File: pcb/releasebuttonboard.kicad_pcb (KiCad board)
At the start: 2 copper layers, 65 x 56 mm, 30 parts, among them SW1 ROTENC, U1 24C16, U2 RASPIPLUSHEADER, U3 OLEDHeader, U4 REncHeader, U5 BtnHeader, U6 PAM8407, U7 REncHeader

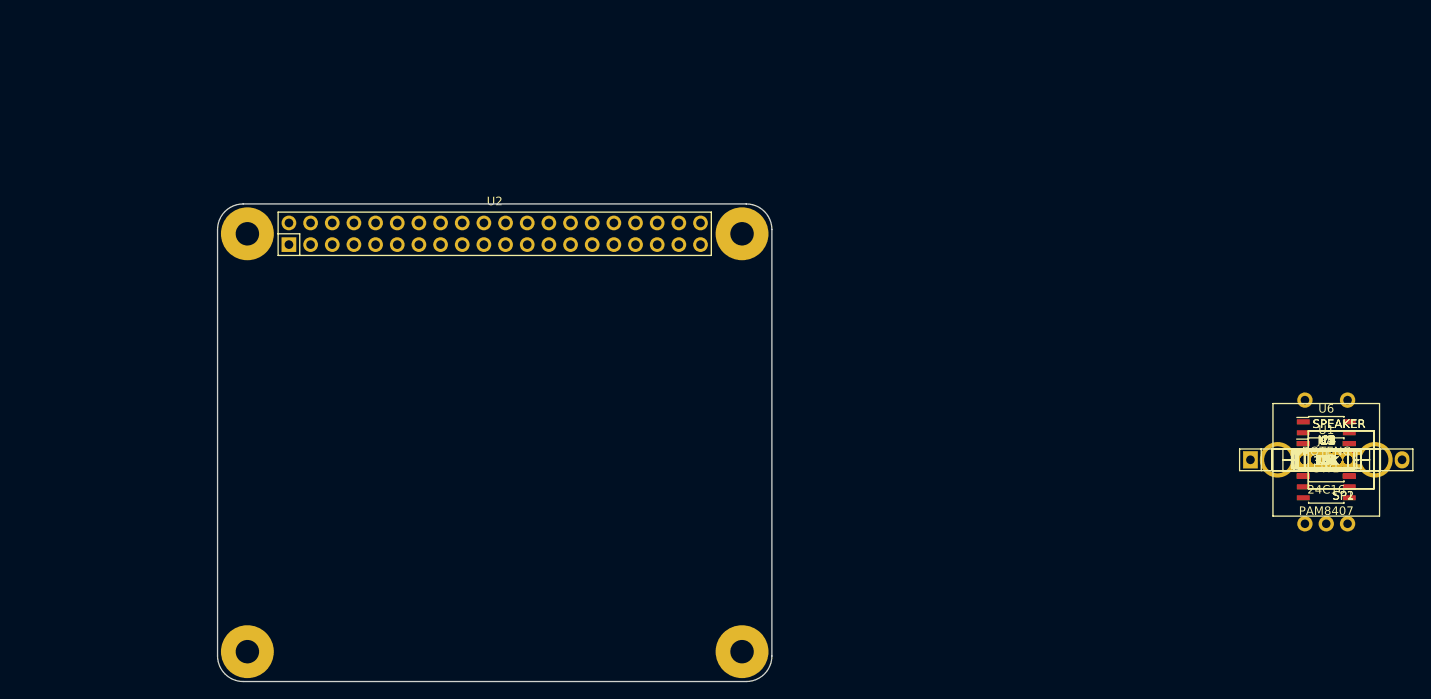
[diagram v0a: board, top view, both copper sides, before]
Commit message: Initial component layout for the audio part of the PCB.
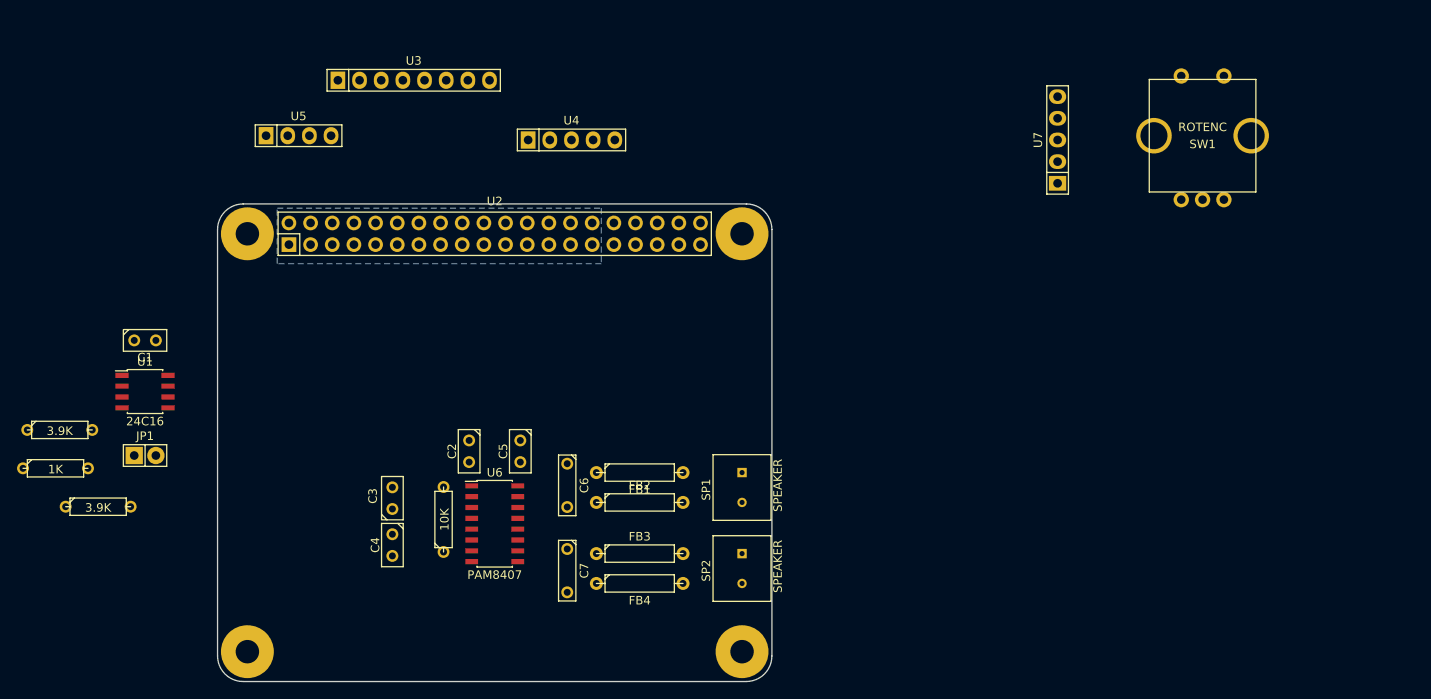
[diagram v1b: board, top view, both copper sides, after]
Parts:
- moved R1 149.0 mm to (76.5, 99.0)
- moved R2 148.5 mm to (77.0, 94.5)
- moved R3 144.1 mm to (81.5, 103.5)
- moved C1 139.2 mm to (87.0, 84.0)
- moved U1 138.7 mm to (87.0, 90.0)
- moved JP1 138.5 mm to (87.0, 97.5)
- moved U5 126.4 mm to (105.0, 60.0)
- moved U3 115.9 mm to (118.5, 53.5)
- moved C4 110.0 mm to (116.0, 108.0), turned to 270 degrees
- moved C3 109.6 mm to (116.0, 102.5), turned to 90 degrees
- moved R4 103.7 mm to (122.0, 105.0), turned to 90 degrees
- moved C2 100.5 mm to (125.0, 97.0), turned to 270 degrees
- moved U6 97.8 mm to (128.0, 105.5)
- moved U4 96.1 mm to (137.0, 60.5)
- moved C5 94.5 mm to (131.0, 97.0), turned to 270 degrees
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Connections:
- SP1 pad 2: Net-(SP1-Pad2) -> Net-(FB2-Pad2)
- SP2 pad 2: Net-(SP2-Pad2) -> Net-(FB4-Pad2)
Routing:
- added copper zone on B.Cu, net GND

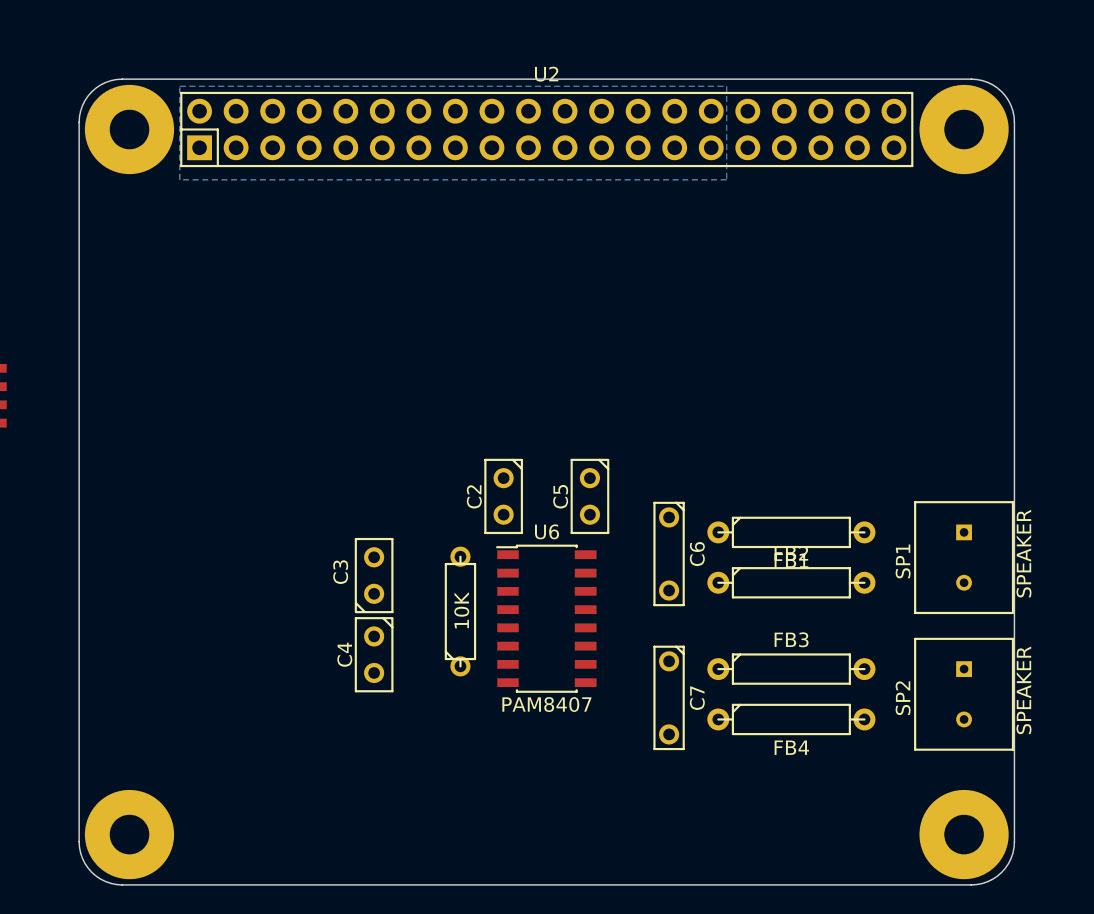
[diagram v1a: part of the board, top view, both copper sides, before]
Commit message: Add separate ground pours for analog and digital.
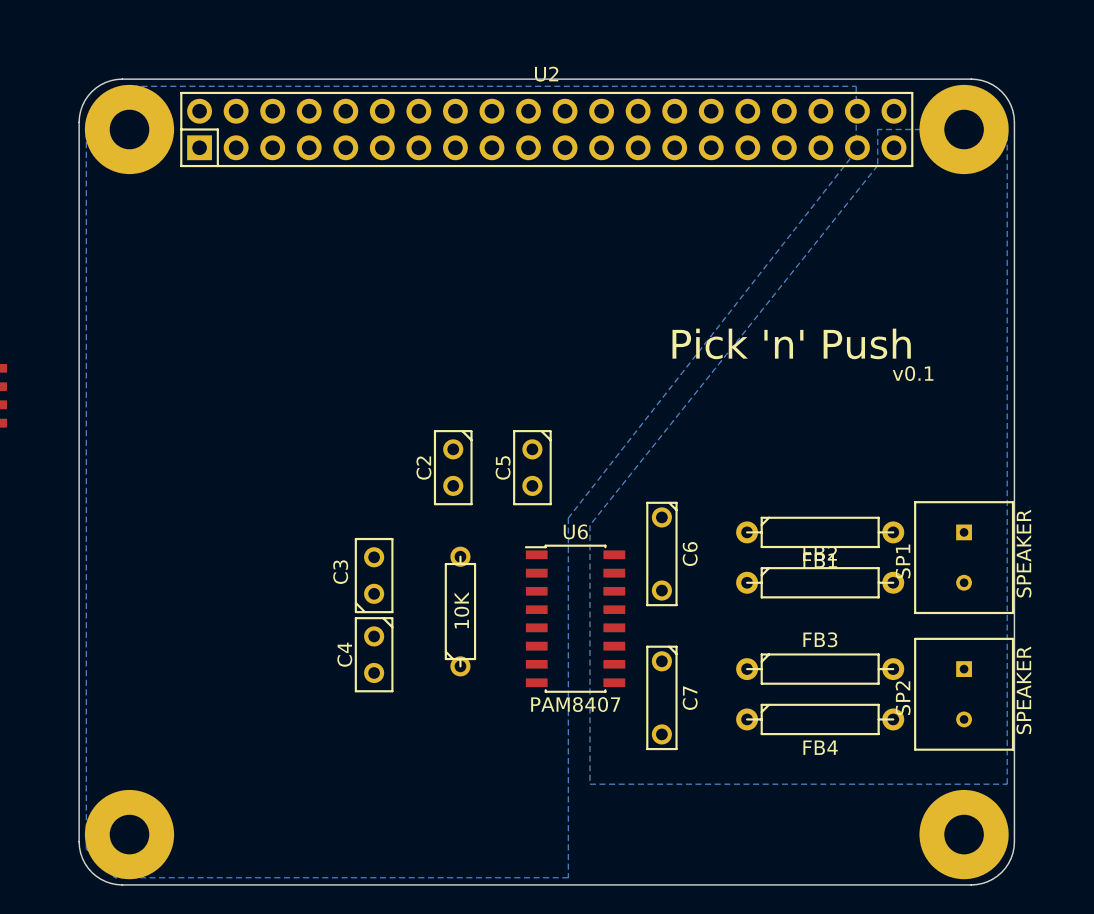
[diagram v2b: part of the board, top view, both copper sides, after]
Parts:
- moved C5 4.47 mm to (127.0, 95.0)
- moved C2 4.03 mm to (121.5, 95.0)
- moved FB1 2.00 mm to (147.0, 99.5)
- moved FB2 2.00 mm to (147.0, 103.0)
- moved FB3 2.00 mm to (147.0, 109.0)
- moved FB4 2.00 mm to (147.0, 112.5)
- moved U6 2.00 mm to (130.0, 105.5)
- moved C6 0.50 mm to (136.0, 101.0)
- moved C7 0.50 mm to (136.0, 111.0)
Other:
- board text added: "Pick 'n' Push"
- board text added: "v0.1"
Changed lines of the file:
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@@
   (general
     (links 75)
-    (no_connects 71)
+    (no_connects 66)
     (area 95.449999 67.949999 160.550001 124.050001)
     (thickness 1.6)
-    (drawings 8)
+    (drawings 10)
     (tracks 0)
     (zones 0)
@@
   )
   (module Discret:C1 (layer F.Cu)
-    (at 125 97 270)
+    (at 121.5 95 270)
     (descr "Condensateur e = 1 pas")
     (tags C)
@@
   )
   (module Discret:C1 (layer F.Cu)
-    (at 131 97 270)
+    (at 127 95 270)
     (descr "Condensateur e = 1 pas")
     (tags C)
@@
   )
   (module Discret:C2 (layer F.Cu)
-    (at 136.5 101 270)
+    (at 136 101 270)
     (descr "Condensateur = 2 pas")
     (tags C)
@@
   )
   (module Discret:C2 (layer F.Cu)
-    (at 136.5 111 270)
+    (at 136 111 270)
     (descr "Condensateur = 2 pas")
     (tags C)
@@
   )
   (module Discret:R4 (layer F.Cu)
-    (at 145 99.5)
+    (at 147 99.5)
     (descr "Resitance 4 pas")
     (tags R)
@@
   )
   (module Discret:R4 (layer F.Cu)
-    (at 145 103)
+    (at 147 103)
     (descr "Resitance 4 pas")
     (tags R)
@@
   )
   (module Discret:R4 (layer F.Cu)
-    (at 145 109)
+    (at 147 109)
     (descr "Resitance 4 pas")
     (tags R)
@@
   )
   (module Discret:R4 (layer F.Cu)
-    (at 145 112.5)
+    (at 147 112.5)
     (descr "Resitance 4 pas")
     (tags R)
@@
   )
   (module SOIC_Packages:SOIC-16_3.9x9.9mm_Pitch1.27mm (layer F.Cu)
-    (at 128 105.5)
+    (at 130 105.5)
     (descr "16-Lead Plastic Small Outline (SL) - Narrow, 3.90 mm Body [SOIC] (see Microchip Packaging Specification 00000049BS.pdf)")
     (tags "SOIC 1.27")
@@
     (pad 1 thru_hole circle (at 0 0) (size 6.2 6.2) (drill 2.75) (layers *.Cu *.Mask F.SilkS))
   )
+  (gr_text v0.1 (at 153.5 88.5) (layer F.SilkS)
+    (effects (font (size 1 1) (thickness 0.25)))
+  )
+  (gr_text "Pick 'n' Push" (at 145 86.5) (layer F.SilkS)
+    (effects (font (size 2 2) (thickness 0.3)))
+  )
   (gr_line (start 160.5 71) (end 160.5 121) (angle 90) (layer Edge.Cuts) (width 0.1))
   (gr_arc (start 157.5 71) (end 157.5 68) (angle 90) (layer Edge.Cuts) (width 0.1))
@@
     (polygon
       (pts
-        (xy 140.5 68.5) (xy 140.5 75) (xy 102.5 75) (xy 102.5 68.5)
+        (xy 151 71.5) (xy 151 74) (xy 131 99) (xy 131 117) (xy 160 117)
+        (xy 160 71.5)
       )
     )
+  )
+  (zone (net 1) (net_name GND) (layer B.Cu) (hatch edge 0.508)
+    (connect_pads (clearance 0.508))
+    (min_thickness 0.254)
+    (fill yes (arc_segments 16) (thermal_gap 0.508) (thermal_bridge_width 0.508))
+    (polygon
+      (pts
+        (xy 149.5 68.5) (xy 149.5 73) (xy 129.5 98.5) (xy 129.5 123.5) (xy 98 123.5)
+        (xy 96 121.5) (xy 96 71) (xy 98.5 68.5)
+      )
+    )

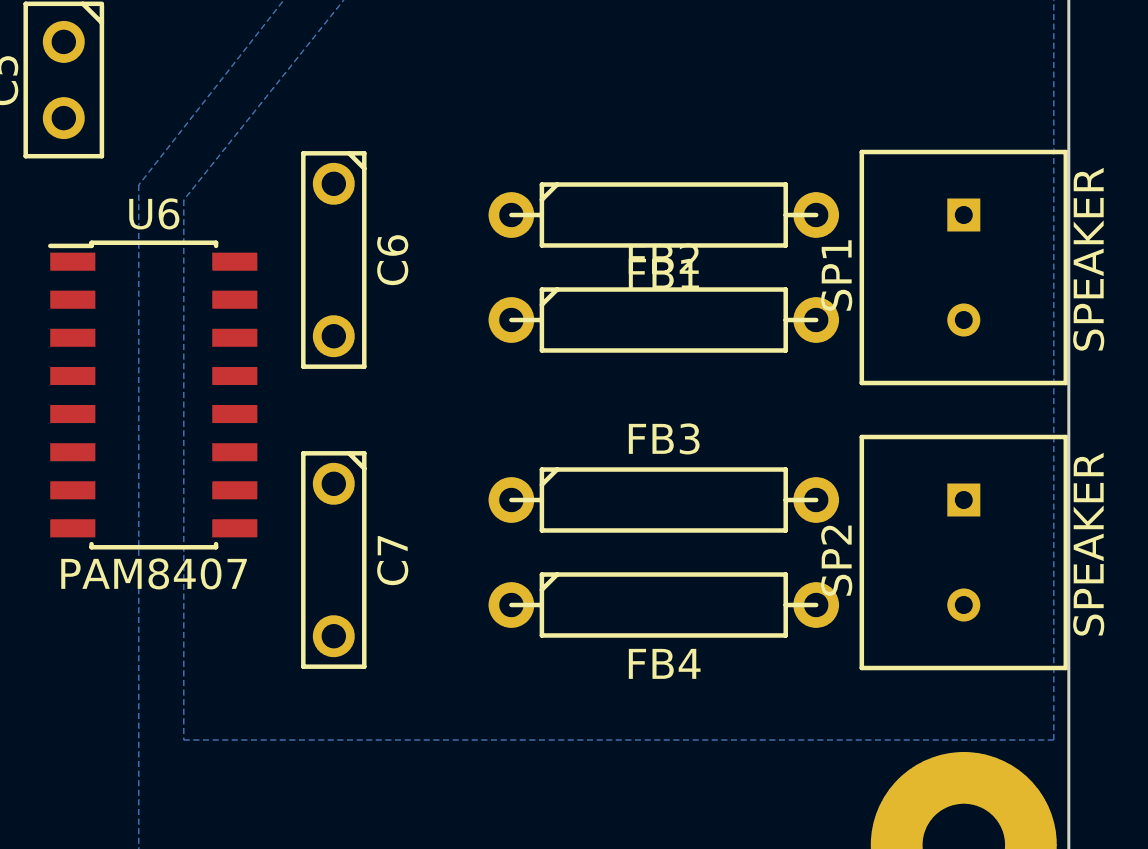
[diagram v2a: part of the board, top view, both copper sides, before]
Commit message: Route the analog part of the PCB.
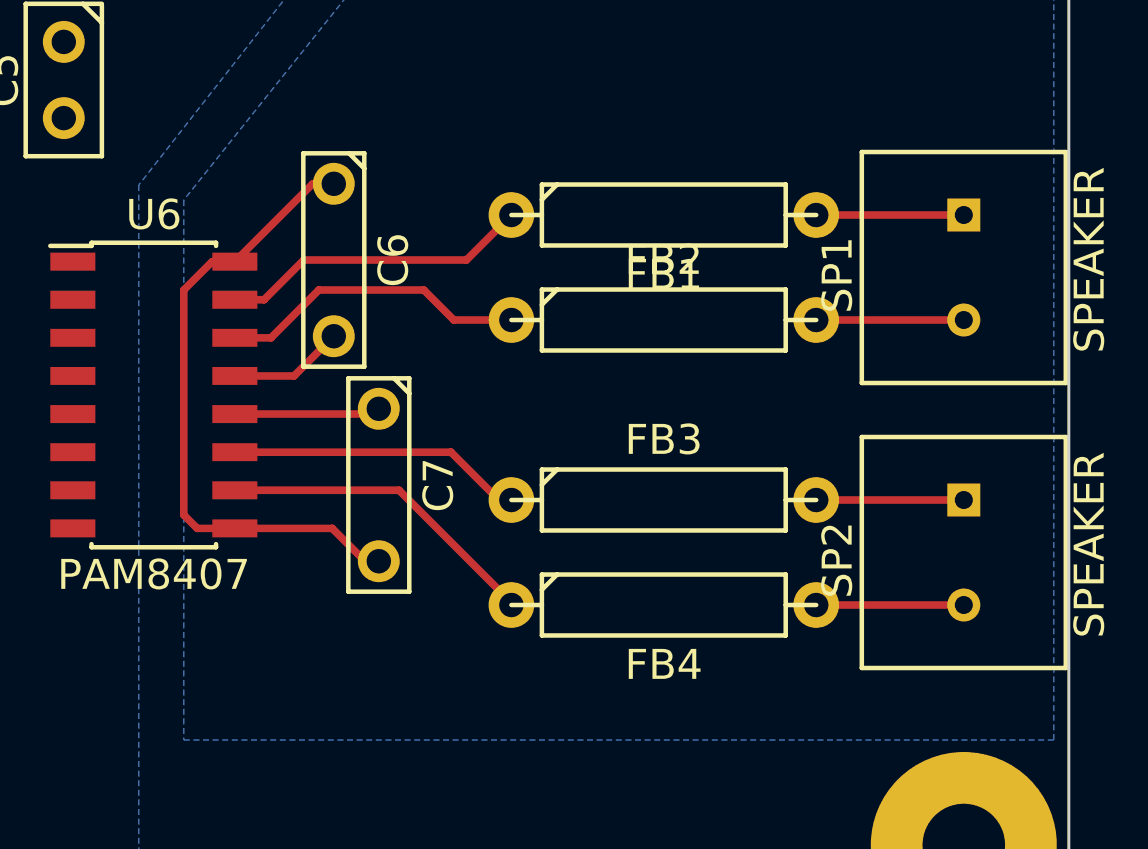
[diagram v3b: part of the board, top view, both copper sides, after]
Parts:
- moved C7 2.92 mm to (137.5, 108.5)
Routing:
- net VCC: track 0.00 -> 21.1 mm
- net Net-(FB4-Pad1): track 0.00 -> 10.9 mm
- net Net-(FB3-Pad1): track 0.00 -> 10.6 mm
- net Net-(FB1-Pad1): track 0.00 -> 10.4 mm
- net Net-(FB2-Pad1): track 0.00 -> 10.3 mm
- net GND: track 0.00 -> 8.72 mm
- net Net-(FB4-Pad2): track 0.00 -> 4.92 mm
- net Net-(FB3-Pad2): track 0.00 -> 4.92 mm
- net Net-(FB2-Pad2): track 0.00 -> 4.92 mm
- net Net-(FB1-Pad2): track 0.00 -> 4.92 mm
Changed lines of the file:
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@@
   (general
     (links 75)
-    (no_connects 66)
+    (no_connects 53)
     (area 95.449999 67.949999 160.550001 124.050001)
     (thickness 1.6)
     (drawings 10)
-    (tracks 0)
+    (tracks 34)
     (zones 0)
     (modules 30)
@@
   )
   (module Discret:C2 (layer F.Cu)
-    (at 136 111 270)
+    (at 137.5 108.5 270)
     (descr "Condensateur = 2 pas")
     (tags C)
@@
   (gr_line (start 95.5 71) (end 95.5 121) (angle 90) (layer Edge.Cuts) (width 0.1))
   (gr_arc (start 98.5 71) (end 95.5 71) (angle 90) (layer Edge.Cuts) (width 0.1))
+  (segment (start 132.7 106.135) (end 137.325 106.135) (width 0.254) (layer F.Cu) (net 1))
+  (segment (start 137.325 106.135) (end 137.5 105.96) (width 0.254) (layer F.Cu) (net 1))
+  (segment (start 132.7 104.865) (end 134.675 104.865) (width 0.254) (layer F.Cu) (net 1))
+  (segment (start 134.675 104.865) (end 136 103.54) (width 0.254) (layer F.Cu) (net 1))
+  (segment (start 132.7 101.055) (end 131.945 101.055) (width 0.254) (layer F.Cu) (net 2))
+  (segment (start 131.445 109.945) (end 132.7 109.945) (width 0.254) (layer F.Cu) (net 2))
+  (segment (start 131 109.5) (end 131.445 109.945) (width 0.254) (layer F.Cu) (net 2))
+  (segment (start 131 102) (end 131 109.5) (width 0.254) (layer F.Cu) (net 2))
+  (segment (start 131.945 101.055) (end 131 102) (width 0.254) (layer F.Cu) (net 2))
+  (segment (start 136 98.46) (end 135.295 98.46) (width 0.254) (layer F.Cu) (net 2))
+  (segment (start 135.295 98.46) (end 132.7 101.055) (width 0.254) (layer F.Cu) (net 2))
+  (segment (start 137.5 111.04) (end 137.04 111.04) (width 0.254) (layer F.Cu) (net 2))
+  (segment (start 137.04 111.04) (end 135.945 109.945) (width 0.254) (layer F.Cu) (net 2))
+  (segment (start 135.945 109.945) (end 132.7 109.945) (width 0.254) (layer F.Cu) (net 2))
+  (segment (start 132.7 102.325) (end 133.675 102.325) (width 0.254) (layer F.Cu) (net 9))
+  (segment (start 140.42 101) (end 141.92 99.5) (width 0.254) (layer F.Cu) (net 9))
+  (segment (start 135 101) (end 140.42 101) (width 0.254) (layer F.Cu) (net 9))
+  (segment (start 133.675 102.325) (end 135 101) (width 0.254) (layer F.Cu) (net 9))
+  (segment (start 157 99.5) (end 152.08 99.5) (width 0.254) (layer F.Cu) (net 10))
+  (segment (start 141.92 103) (end 140 103) (width 0.254) (layer F.Cu) (net 11))
+  (segment (start 133.905 103.595) (end 132.7 103.595) (width 0.254) (layer F.Cu) (net 11))
+  (segment (start 135.5 102) (end 133.905 103.595) (width 0.254) (layer F.Cu) (net 11))
+  (segment (start 139 102) (end 135.5 102) (width 0.254) (layer F.Cu) (net 11))
+  (segment (start 140 103) (end 139 102) (width 0.254) (layer F.Cu) (net 11))
+  (segment (start 157 103) (end 152.08 103) (width 0.254) (layer F.Cu) (net 12))
+  (segment (start 141.92 109) (end 141.5 109) (width 0.254) (layer F.Cu) (net 13))
+  (segment (start 141.5 109) (end 139.905 107.405) (width 0.254) (layer F.Cu) (net 13))
+  (segment (start 139.905 107.405) (end 132.7 107.405) (width 0.254) (layer F.Cu) (net 13))
+  (segment (start 132.7 107.405) (end 133.405 107.405) (width 0.254) (layer F.Cu) (net 13))
+  (segment (start 157 109) (end 152.08 109) (width 0.254) (layer F.Cu) (net 14))
+  (segment (start 141.92 112.5) (end 141.92 112.42) (width 0.254) (layer F.Cu) (net 15))
+  (segment (start 141.92 112.42) (end 138.175 108.675) (width 0.254) (layer F.Cu) (net 15))
+  (segment (start 138.175 108.675) (end 132.7 108.675) (width 0.254) (layer F.Cu) (net 15))
+  (segment (start 157 112.5) (end 152.08 112.5) (width 0.254) (layer F.Cu) (net 16))
   (zone (net 1) (net_name GND) (layer B.Cu) (hatch edge 0.508)
     (connect_pads (clearance 0.508))
